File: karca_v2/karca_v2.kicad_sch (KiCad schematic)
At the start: 4 parts

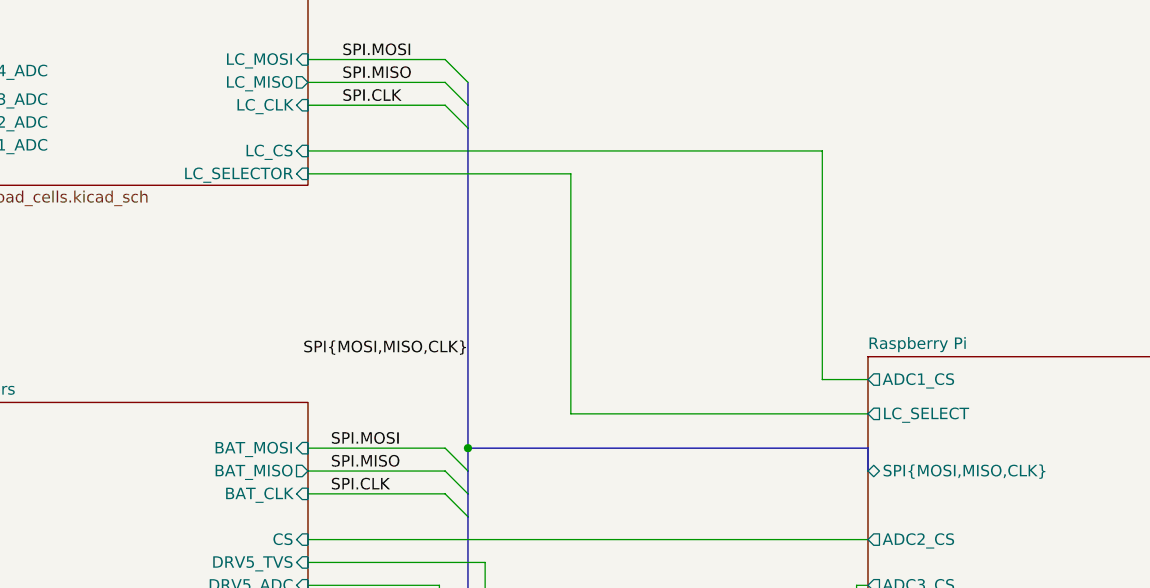
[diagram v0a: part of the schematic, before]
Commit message: replaced digital switches with jumpers, simpler design
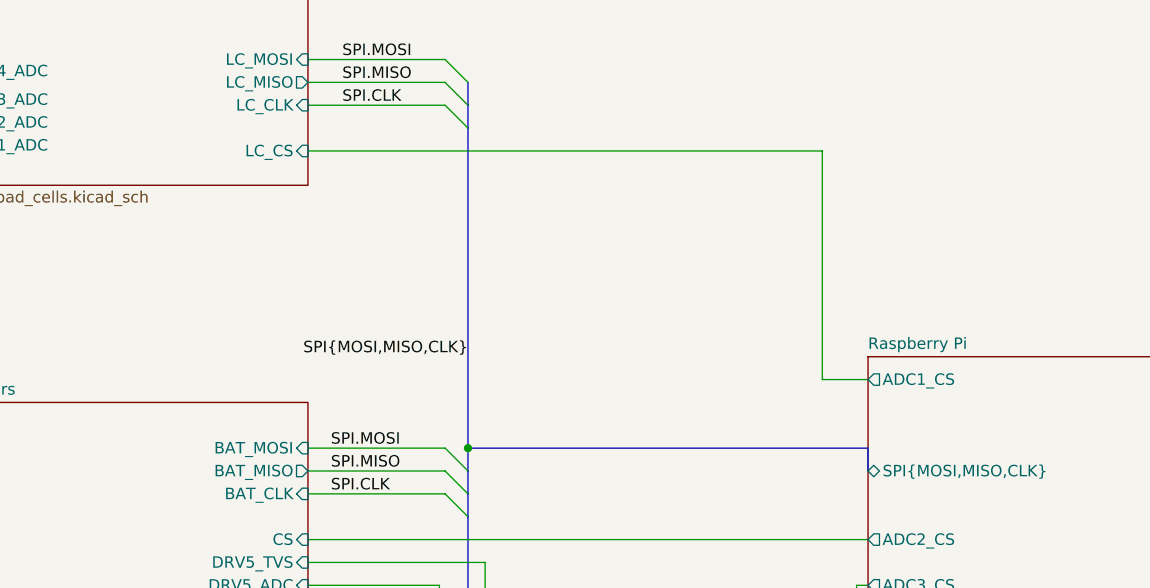
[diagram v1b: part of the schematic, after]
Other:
- sheet Load Cells ports: added none; removed LC_SELECTOR
- sheet Raspberry Pi ports: added none; removed LC_SELECT
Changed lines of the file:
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@@
-    (stroke (width 0) (type default))
-  )
-  (wire (pts (xy 127 102.87) (xy 160.02 102.87))
     (stroke (width 0) (type default))
   )
@@
     (stroke (width 0) (type default))
   )
-  (wire (pts (xy 127 76.2) (xy 97.79 76.2))
-    (stroke (width 0) (type default))
-  )
   (wire (pts (xy 207.01 116.84) (xy 215.9 116.84))
     (stroke (width 0) (type default))
@@
   )
   (wire (pts (xy 160.02 121.92) (xy 158.75 121.92))
-    (stroke (width 0) (type default))
-  )
-  (wire (pts (xy 127 102.87) (xy 127 76.2))
     (stroke (width 0) (type default))
   )
@@
       (effects (font (size 1.27 1.27)) (justify left top))
     )
-    (pin "LC_SELECTOR" input (at 97.79 76.2 0)
-      (effects (font (size 1.27 1.27)) (justify right))
-    )
     (pin "LC_CLK" input (at 97.79 68.58 0)
       (effects (font (size 1.27 1.27)) (justify right))
@@
       (effects (font (size 1.27 1.27)) (justify left))
     )
-    (pin "LC_SELECT" output (at 160.02 102.87 180)
-      (effects (font (size 1.27 1.27)) (justify left))
-    )

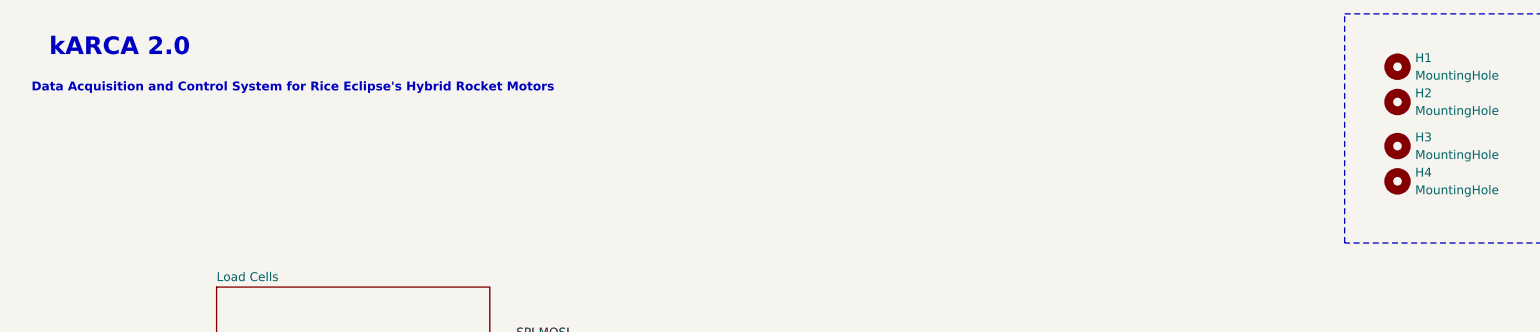
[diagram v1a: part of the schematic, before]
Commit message: cleaned up documentation. Added production files and BOM. Marked Thermocouple components and THT components as DNP (excluded them from BOM too) to match version sent to JLCPCB for fabrication
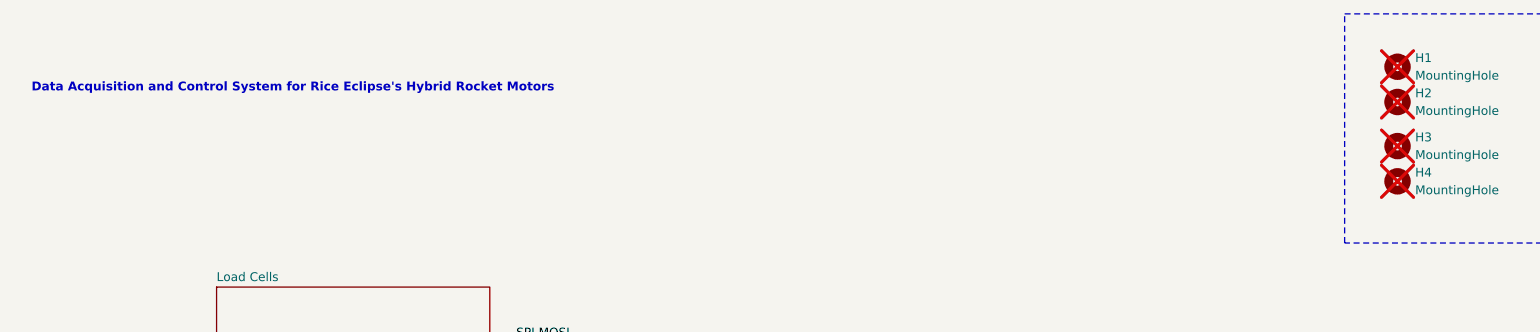
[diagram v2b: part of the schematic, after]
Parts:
- H1, H2, H3, H4: now not fitted; now left out of the parts list
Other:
- note removed: "kARCA 2.0"
- company: (none) -> Rice Eclipse
- title: (none) -> kARCA 2.0 Engine Control System
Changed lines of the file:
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@@
 (kicad_sch (version 20230121) (generator eeschema)
   (paper "A4")
+  (title_block
+    (title "kARCA 2.0 Engine Control System")
+    (date "2024-12-16")
+    (rev "1.1")
+    (company "Rice Eclipse")
+    (comment 1 "Designed by Deepak Narayan")
+    (comment 2 "Engine Control System for the Static Engine Testing of Rice Eclipse's Hybrid Rocket Motors")
+  )
   (junction (at 115.57 106.68) (diameter 0) (color 0 0 0 0)
   )
@@
     (effects (font (size 1.27 1.27)) (justify left bottom))
   )
-  (text "kARCA 2.0" (at 34.29 22.86 0)
-    (effects (font (size 2.54 2.54) (thickness 0.508) bold) (justify left bottom))
-  )
   (text "Data Acquisition and Control System for Rice Eclipse's Hybrid Rocket Motors"
     (at 31.75 27.94 0)
@@
   )
   (symbol (lib_id "Mechanical:MountingHole") (at 228.6 24.13 0) (unit 1)
-    (in_bom yes) (on_board yes) (dnp no)
+    (in_bom no) (on_board yes) (dnp yes)
     (property "Reference" "H1" (at 231.14 22.86 0)
       (effects (font (size 1.27 1.27)) (justify left))
@@
   )
   (symbol (lib_id "Mechanical:MountingHole") (at 228.6 35.56 0) (unit 1)
-    (in_bom yes) (on_board yes) (dnp no) (fields_autoplaced)
+    (in_bom no) (on_board yes) (dnp yes) (fields_autoplaced)
     (property "Reference" "H3" (at 231.14 34.29 0)
       (effects (font (size 1.27 1.27)) (justify left))
@@
   )
   (symbol (lib_id "Mechanical:MountingHole") (at 228.6 29.21 0) (unit 1)
-    (in_bom yes) (on_board yes) (dnp no) (fields_autoplaced)
+    (in_bom no) (on_board yes) (dnp yes) (fields_autoplaced)
     (property "Reference" "H2" (at 231.14 27.94 0)
       (effects (font (size 1.27 1.27)) (justify left))
@@
   )
   (symbol (lib_id "Mechanical:MountingHole") (at 228.6 40.64 0) (unit 1)
-    (in_bom yes) (on_board yes) (dnp no) (fields_autoplaced)
+    (in_bom no) (on_board yes) (dnp yes) (fields_autoplaced)
     (property "Reference" "H4" (at 231.14 39.37 0)
       (effects (font (size 1.27 1.27)) (justify left))

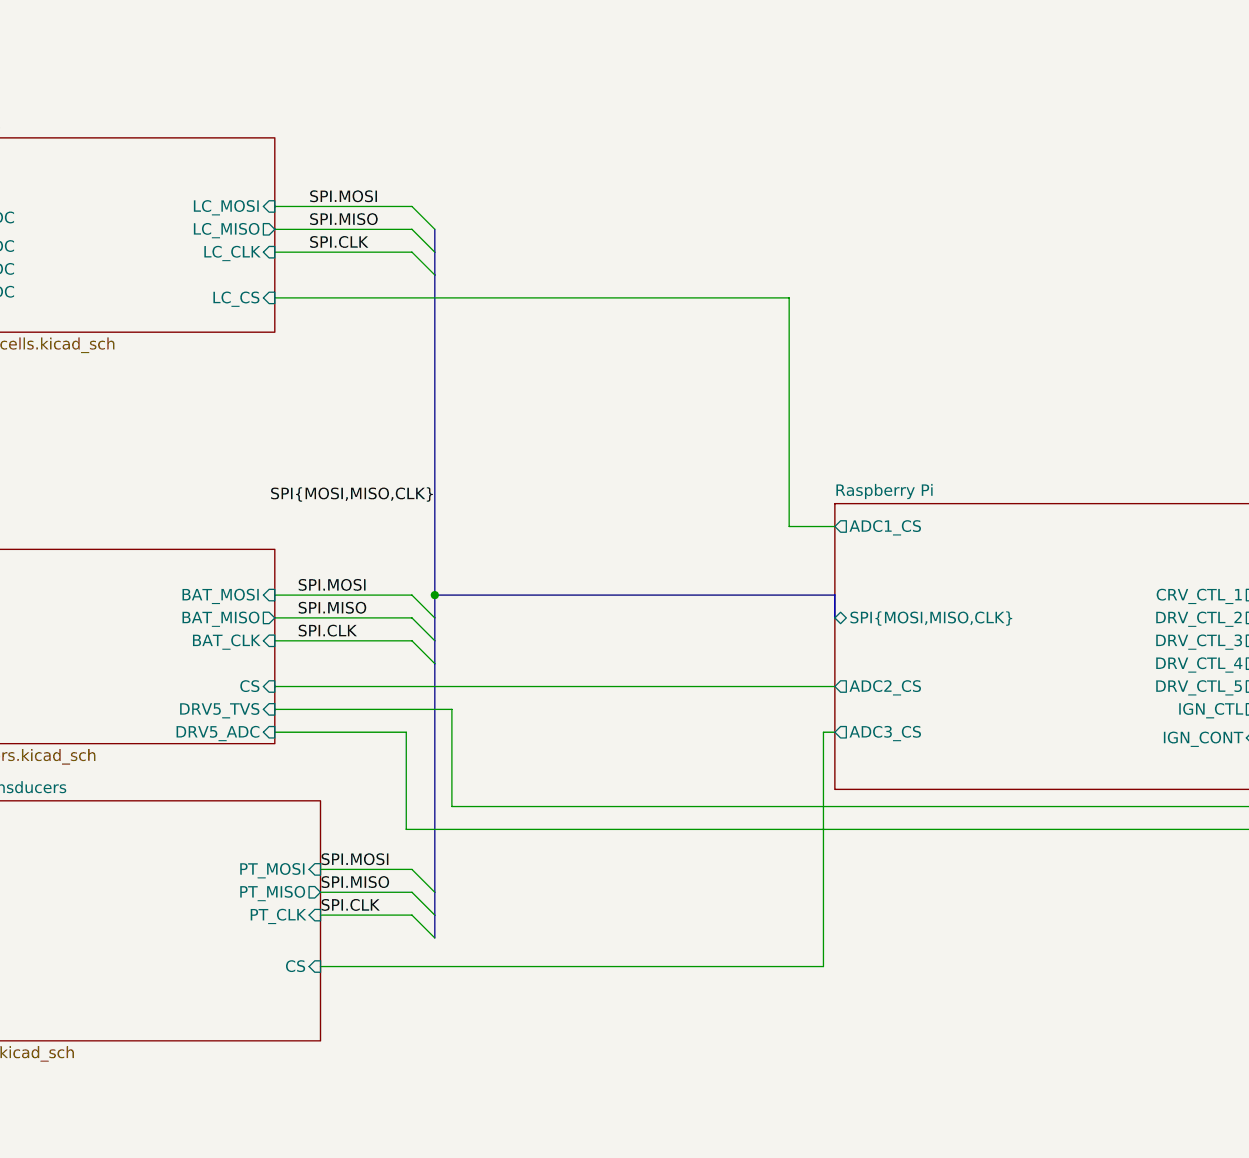
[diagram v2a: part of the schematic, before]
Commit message: new design: chip on board
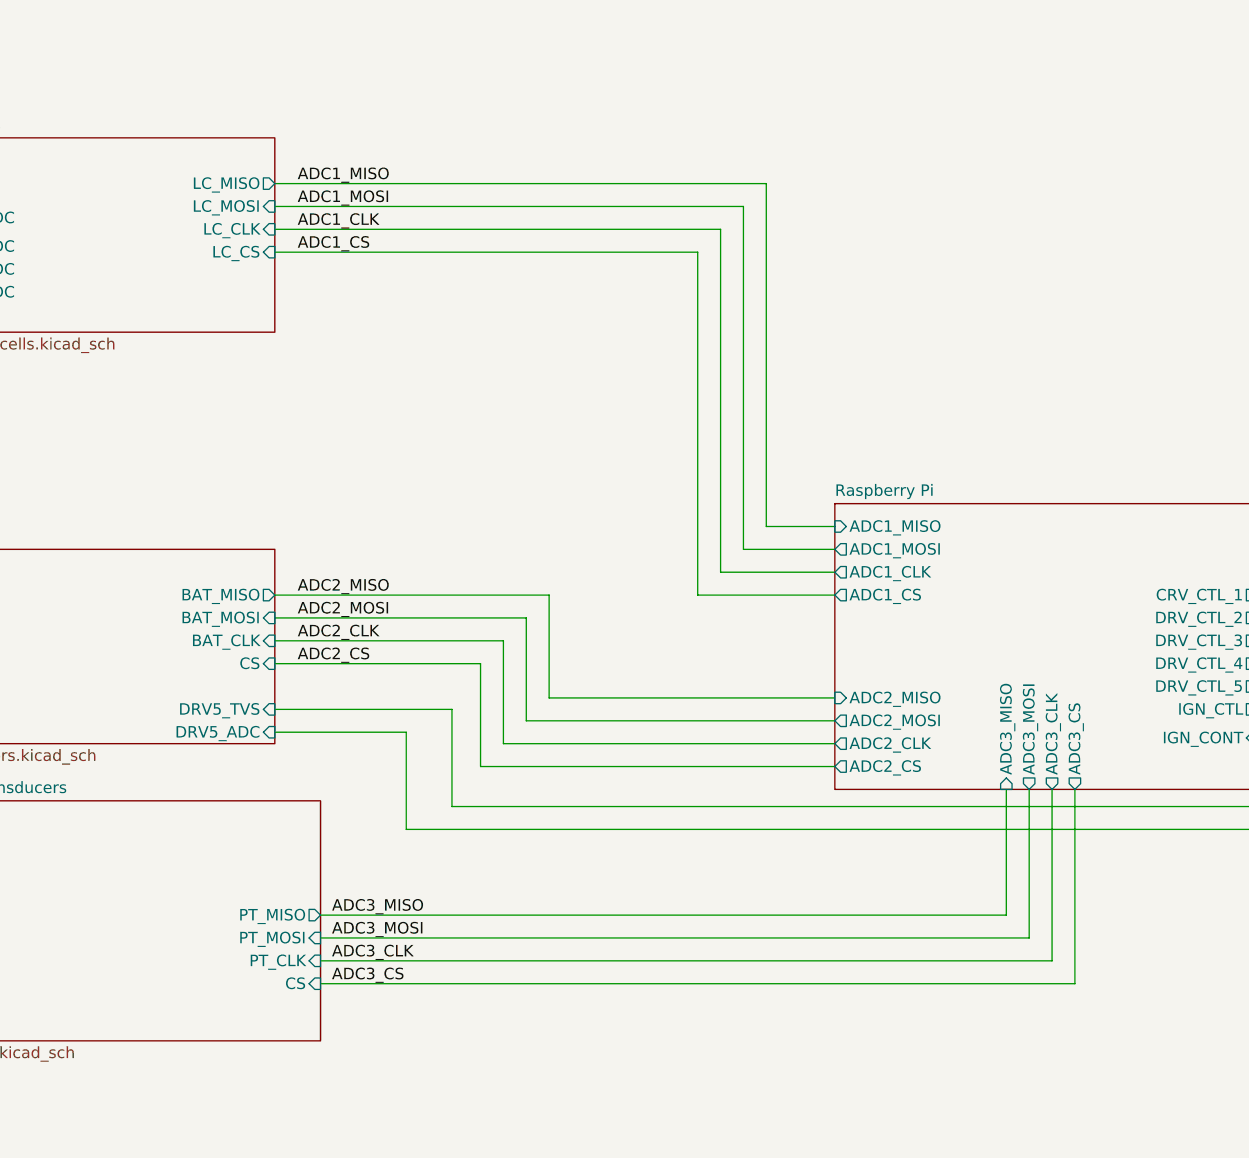
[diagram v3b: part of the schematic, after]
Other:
- sheet Raspberry Pi ports: added ADC1_CLK, ADC1_MISO, ADC1_MOSI, ADC2_CLK, ADC2_MISO, ADC2_MOSI, ADC3_CLK, ADC3_MISO, ADC3_MOSI; removed SPI{MOSI,MISO,CLK}
